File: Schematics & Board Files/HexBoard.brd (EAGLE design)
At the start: 40.4 x 35.6 mm, 26 parts, among them X1 SSW-105-02-S-D-RA

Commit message: New board design
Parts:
- removed X1: SSW-105-02-S-D-RA, con-samtec:TSW-105-02-S-D-RA
- added XTAL: TXC-CRYSTAL, TXC:TXC_CRYSTAL
- C5: value 12p -> 2.2n
- C6: value 12p -> 1p
- C7: value 12p -> 1.5p
- C8: value 12p -> 3.9p
- U$1: value TXC-CRYSTAL -> HEADER.05"PITCH; device TXC:TXC_CRYSTAL -> Headers:HEADER.05"PITCH
- moved U$1 22.2 mm to (50.7, 18.5), turned to 180 degrees
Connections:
- net GND: now also U$1.3, U$1.5, U$1.9, XTAL.2, XTAL.4; no longer U$1.2, U$1.4, X1.3, X1.5, X1.9
- net N$10: now also U$1.2; no longer X1.2
- net N$7: now also U$1.4; no longer X1.4
- net N$8: now also XTAL.3; no longer U$1.3
- net N$9: now also XTAL.1; no longer U$1.1
- net VDD: now also U$1.1; no longer X1.1
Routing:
- net N$7: track 13.9 -> 25.3 mm
- net N$10: track 14.6 -> 22.3 mm
- net GND: vias 90 -> 99

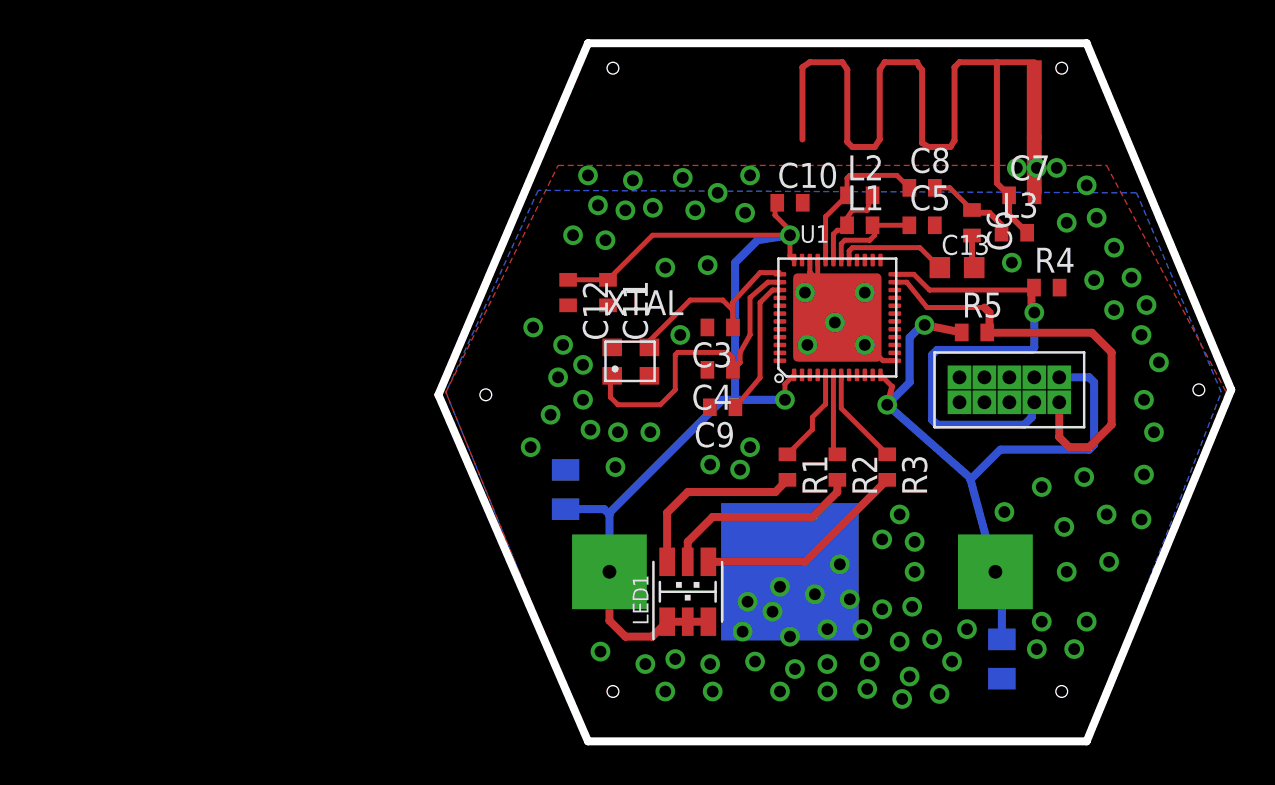
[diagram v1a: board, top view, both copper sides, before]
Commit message: Schematic clean up
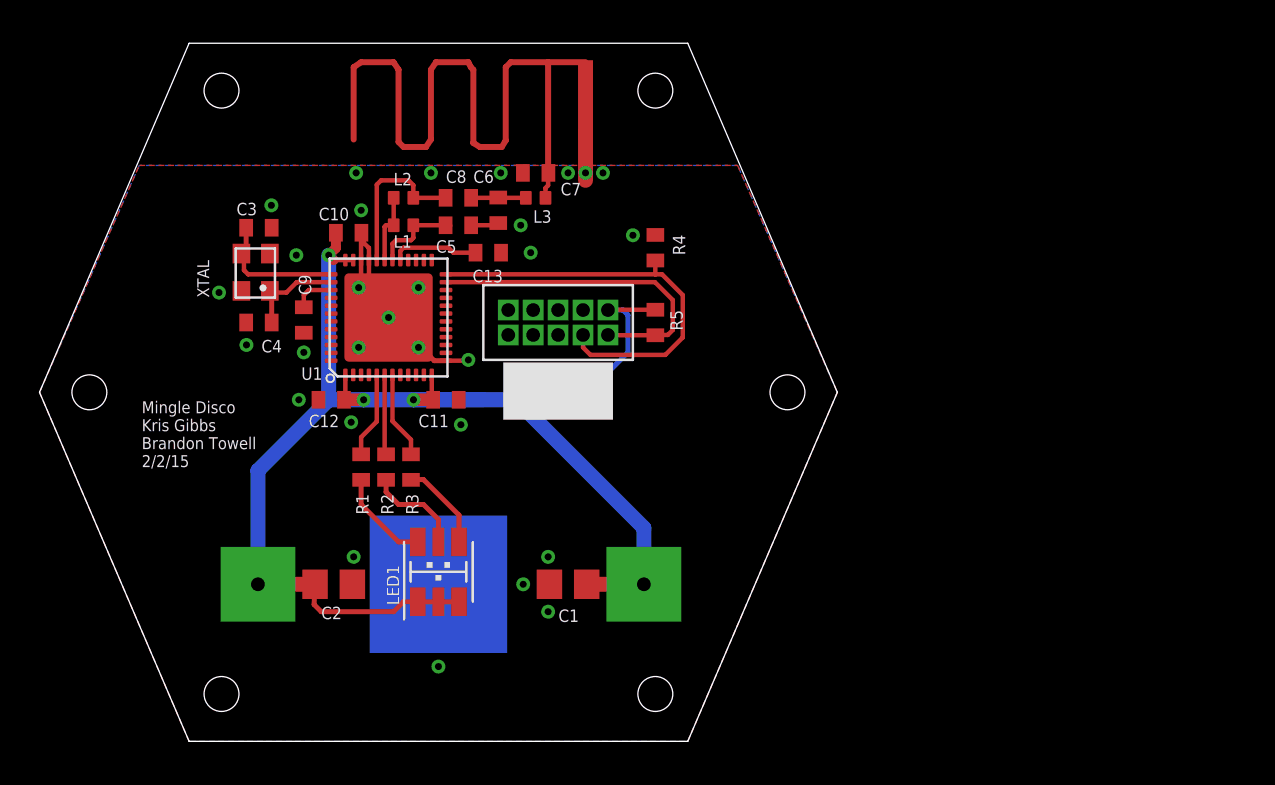
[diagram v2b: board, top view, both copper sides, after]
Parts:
- C1, C2: device adafruit:C0805K -> rcl:C0805
- C10, C11, C12, C3, C4, C5, C6, C7, C8, C9: device adafruit:C0402 -> rcl:C0402
- C13: device adafruit:C0603K -> rcl:C0402
- L1, L2, L3: device CHIP_INDUCTOR:CHIP_INDUCTOR -> rcl_custom:.0402-B-NOSILK
- moved C7 24.8 mm to (25.3, 29.0), turned to 180 degrees
- moved R3 24.3 mm to (18.9, 14.0)
- moved C6 24.1 mm to (23.4, 27.1)
- moved C3 24.0 mm to (11.2, 26.2), turned to 0 degrees
- moved C13 23.9 mm to (22.9, 24.9)
- moved C8 23.6 mm to (21.3, 27.7)
- moved C5 23.6 mm to (21.3, 26.3)
- moved C4 23.6 mm to (11.2, 21.3)
- moved L3 23.5 mm to (25.3, 27.7)
- moved U$1 23.2 mm to (27.7, 22.0)
- moved R2 23.0 mm to (17.7, 14.0)
- moved U1 22.9 mm to (17.8, 21.6)
- moved C10 22.5 mm to (15.7, 25.9)
- moved C1 22.4 mm to (26.9, 8.00), flipped to the top, turned to 180 degrees
- moved L1 22.1 mm to (18.5, 26.3), turned to 180 degrees
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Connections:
- net N$10 renamed !RESET
- net N$7 renamed SWD
- net N$8 renamed XTAL
- net N$11: now also L1.2, L2.1; no longer L1.1, L2.2
- net N$15: now also L2.2; no longer L2.1
- net N$17: now also L1.1; no longer L1.2
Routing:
- net N$9: track 16.2 -> 5.03 mm
- net VDD: track 87.0 -> 78.3 mm, vias 4 -> 3
- net N$3: track 10.8 -> 4.57 mm
- net GND: track 13.0 -> 18.5 mm, vias 99 -> 29
- net !RESET: track 22.3 -> 16.9 mm
- net N$2: track 10.3 -> 5.01 mm
- net N$12: track 7.06 -> 2.12 mm
- net N$1: track 9.33 -> 4.93 mm
- net SWD: track 25.3 -> 21.6 mm, vias 1 -> 0
- net XTAL: track 10.1 -> 7.02 mm
- net ANTENNA: track 40.9 -> 38.5 mm
- net N$13: track 4.58 -> 2.79 mm
- net N$18: track 5.58 -> 4.47 mm
- net N$11: track 4.62 -> 3.59 mm
- net N$17: track 5.15 -> 4.54 mm
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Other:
- board size 40.4 x 35.6 mm -> 40.6 x 35.6 mm
- board text added: "Mingle Disco Kris Gibbs Brandon Towell 2/2/15"
